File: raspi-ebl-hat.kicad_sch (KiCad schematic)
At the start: 3 parts, among them J1 43045-1012, J2 43650-0515, J3 43650-0615

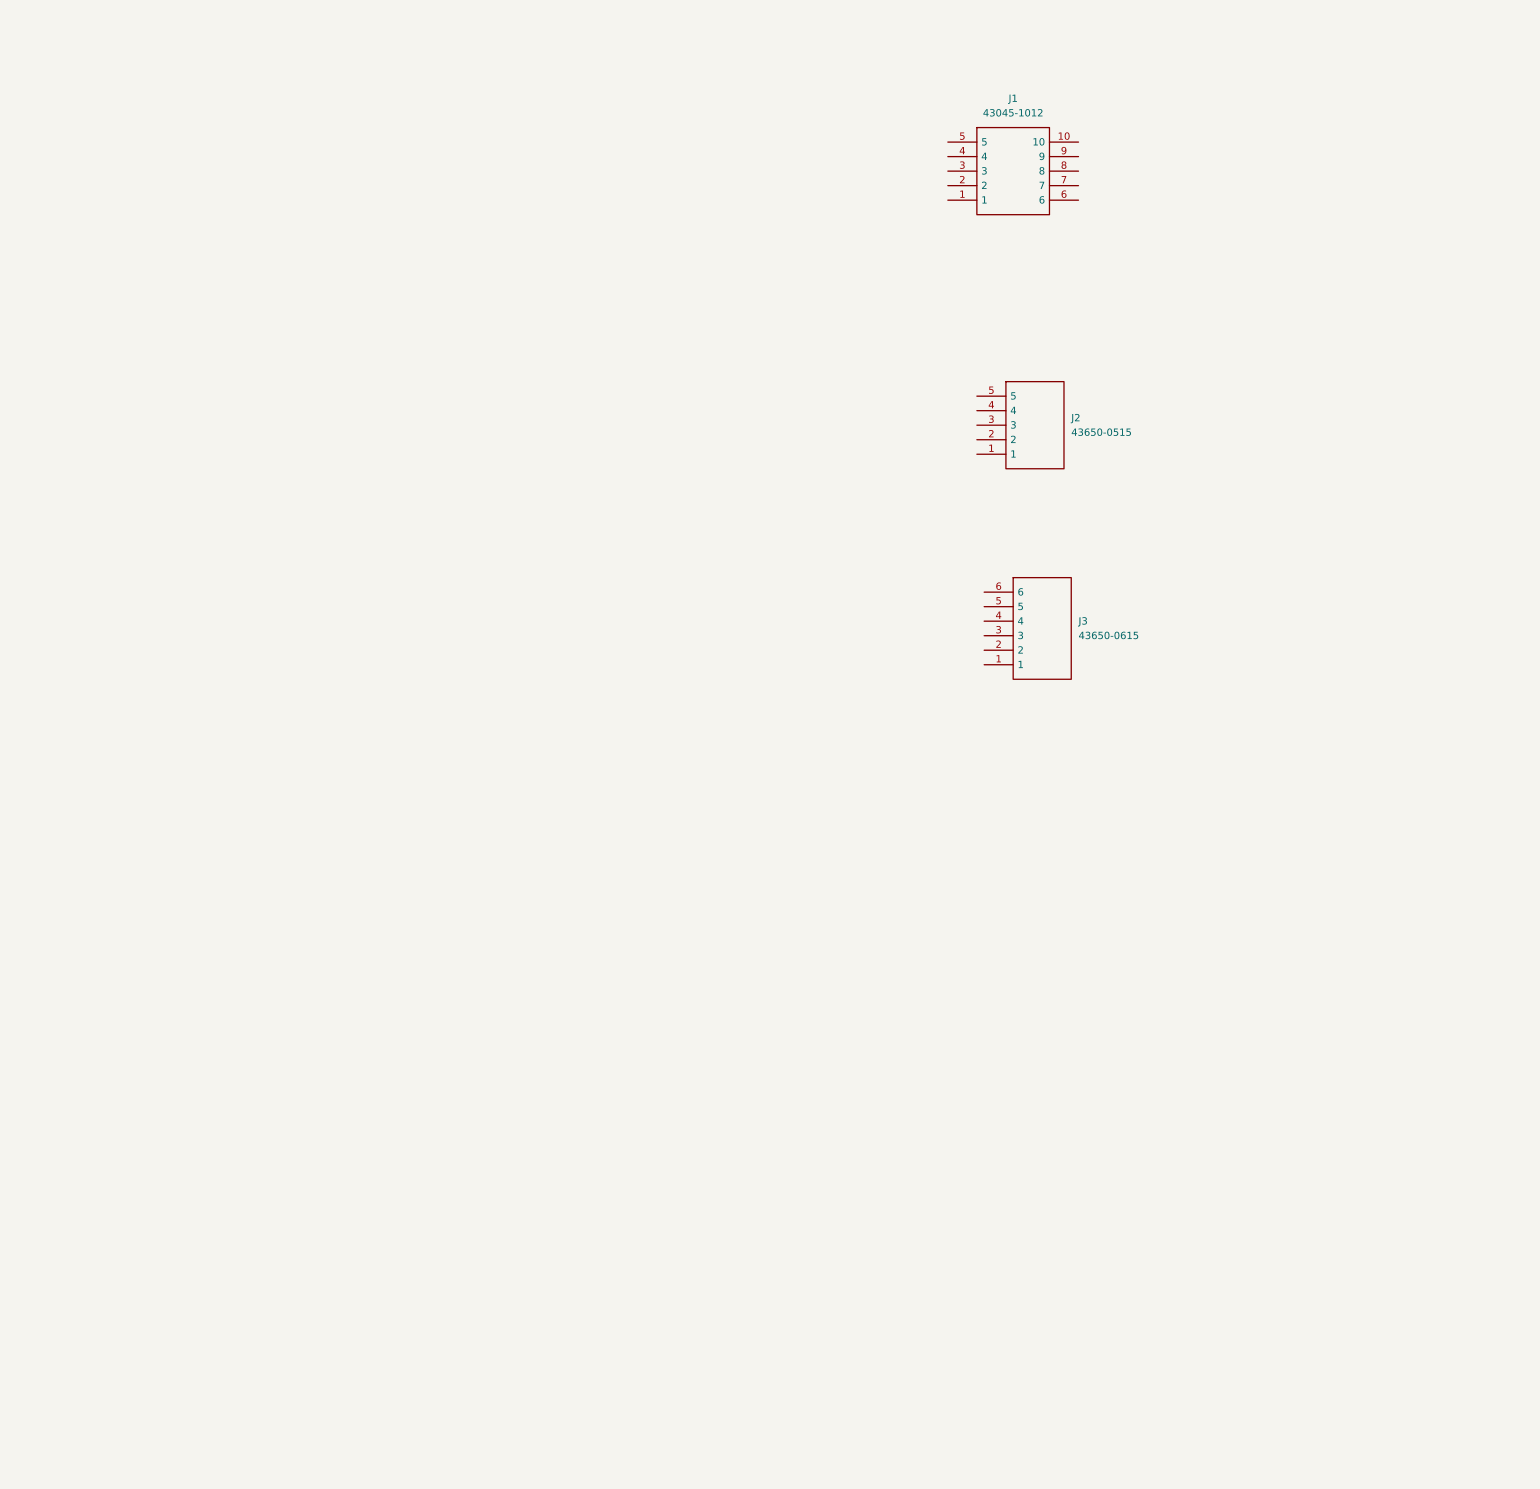
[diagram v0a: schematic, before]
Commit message: imported pihat-template stuff
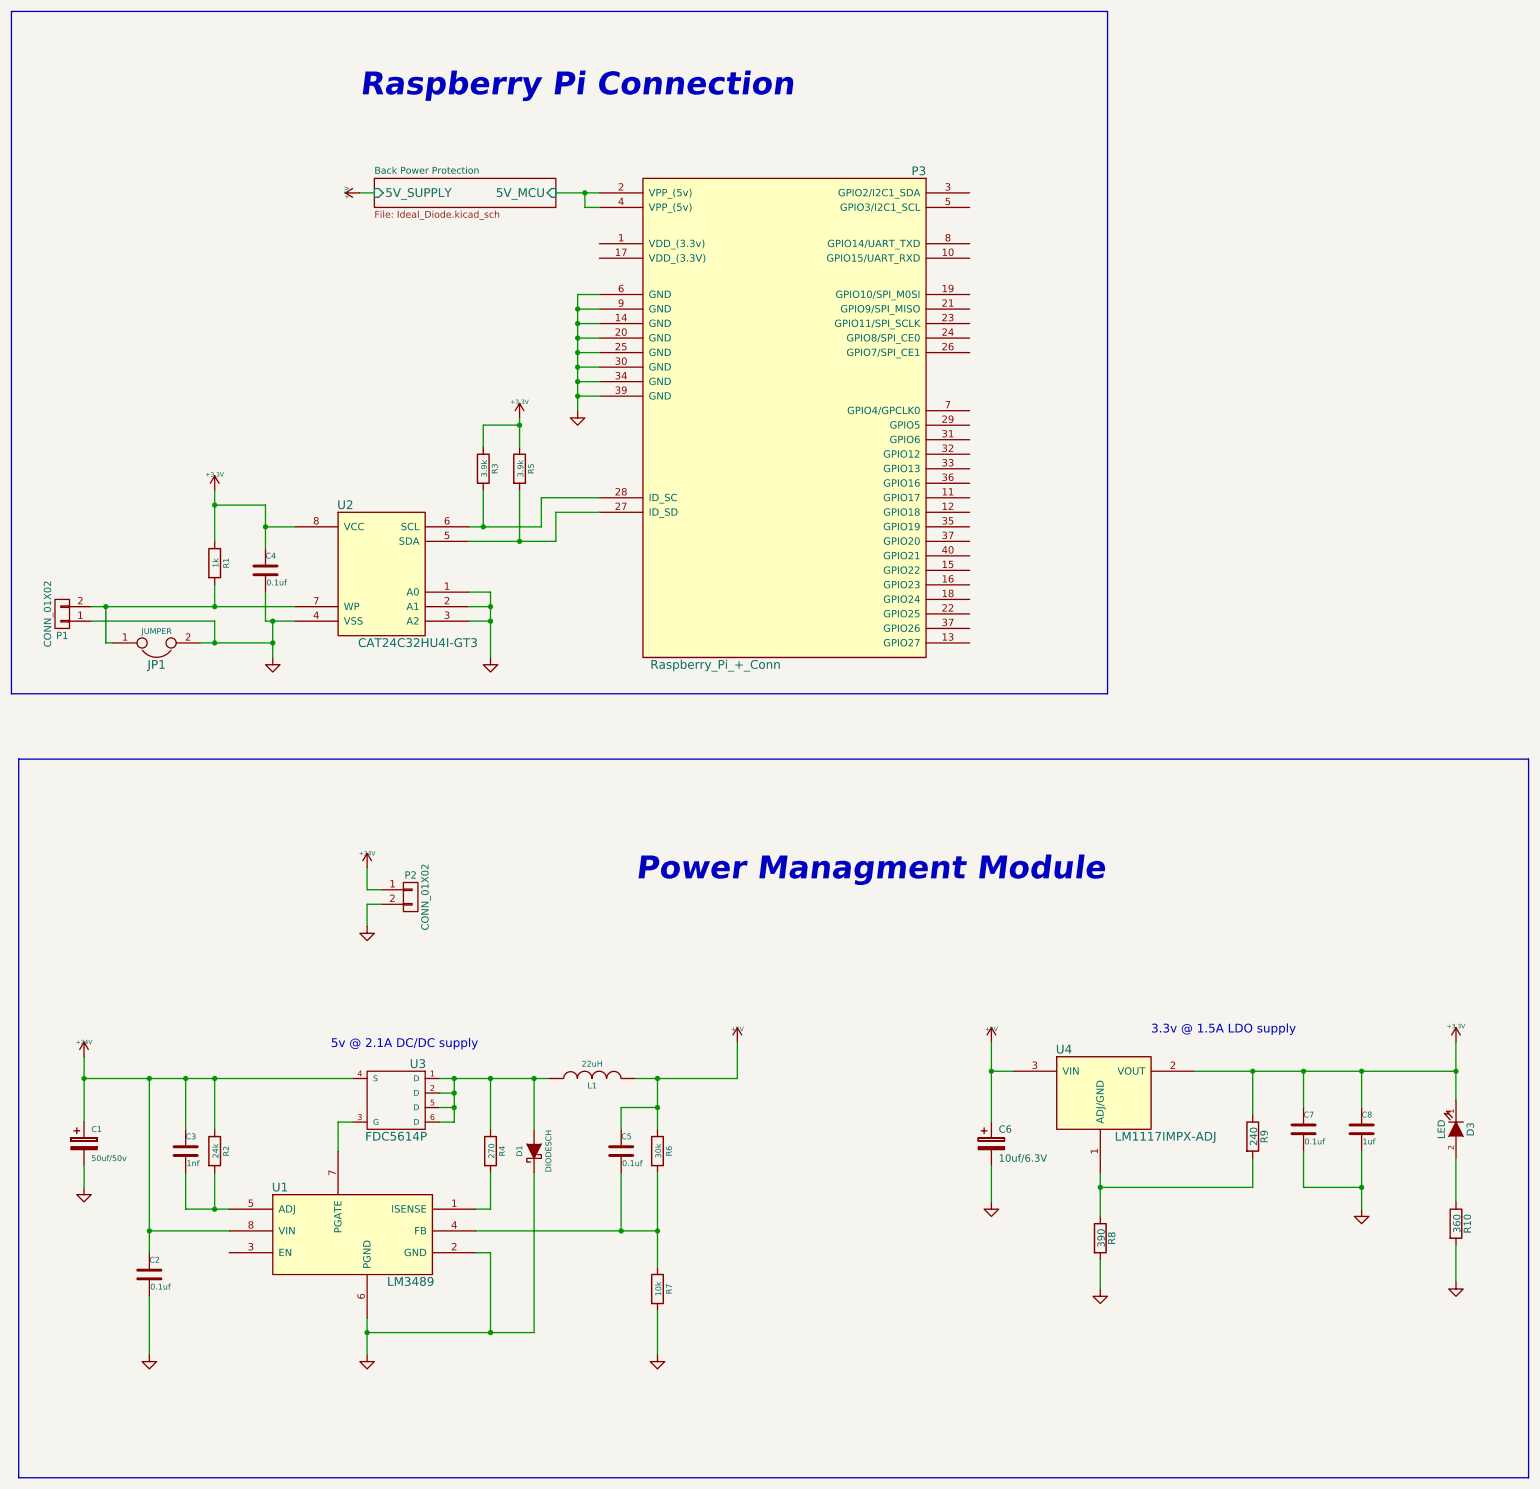
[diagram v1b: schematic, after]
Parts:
- removed J1: 43045-1012, 43045-10YY_12,13,14, symbol parts:43045-1012
- removed J2: 43650-0515, 43650-05YY_15,16,17, symbol parts:43650-0515
- removed J3: 43650-0615, 43650-06YY_15,16,17, symbol parts:43650-0615
- added C1: 50uf/50v, w_smd_cap:c_elec_6.3x7.7, symbol pihat_template-rescue:CP
- added C2, C4, C5, C7: 0.1uf, w_smd_cap:c_0402, symbol pihat_template-rescue:C
- added C3: 1nf, w_smd_cap:c_0402, symbol pihat_template-rescue:C
- added C6: 10uf/6.3V, w_smd_cap:c_elec_4x5.3, symbol pihat_template-rescue:CP
- added C8: 1uf, w_smd_cap:c_0402, symbol pihat_template-rescue:C
- added D1: DIODESCH, w_smd_diode:do214aa, symbol pihat_template-rescue:D_Schottky
- added D3: LED, w_smd_leds:Led_0603, symbol pihat_template-rescue:LED
- added JP1: JUMPER, w_smd_resistors:r_0603, symbol pihat_template-rescue:JUMPER
- added L1: 22uH, w_smd_inductors:inductor_smd_8x5mm, symbol pihat_template-rescue:INDUCTOR
- added P1: CONN_01X02, w_pin_strip:pin_strip_2, symbol pihat_template-rescue:CONN_01X02
- added P2: CONN_01X02, w_conn_mkds:mkds_1,5-2, symbol pihat_template-rescue:CONN_01X02
- added P3: Raspberry_Pi_+_Conn, w_conn_strip:vasch_strip_20x2, symbol pihat_template-rescue:Raspberry_Pi_+_Conn
- added R1: 1k, w_smd_resistors:r_0402, symbol pihat_template-rescue:R
- added R10: 360, w_smd_resistors:r_0402, symbol pihat_template-rescue:R
- added R2: 24k, w_smd_resistors:r_0402, symbol pihat_template-rescue:R
- added R3, R5: 3.9k, w_smd_resistors:r_0402, symbol pihat_template-rescue:R
- added R4: 270, w_smd_resistors:r_0402, symbol pihat_template-rescue:R
- added R6: 30k, w_smd_resistors:r_0402, symbol pihat_template-rescue:R
- added R7: 10k, w_smd_resistors:r_0402, symbol pihat_template-rescue:R
- added R8: 390, w_smd_resistors:r_0402, symbol pihat_template-rescue:R
- added R9: 240, w_smd_resistors:r_0402, symbol pihat_template-rescue:R
- added U1: LM3489, w_smd_dil:msoic-8, symbol pihat_template-rescue:LM3489
- added U2: CAT24C32HU4I-GT3, w_smd_dil:tssop-8, symbol pihat_template-rescue:CAT24C32HU4I-GT3
- added U3: FDC5614P, w_smd_trans:sot23-6, symbol pihat_template-rescue:FDC5614P
- added U4: LM1117IMPX-ADJ, w_smd_trans:sot223, symbol pihat_template-rescue:LM1117IMPX-ADJ
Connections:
- new net: P3.27 (ID_SD), R5.2, U2.5 (SDA)
- new net: P3.28 (ID_SC), R3.2, U2.6 (SCL)
- new net: JP1.1, P1.2 (P2), R1.2, U2.7 (WP)
- new net: R4.2, U1.1 (ISENSE)
- new net: C5.2, R6.2, R7.1, U1.4 (FB)
- new net: C3.2, R2.2, U1.5 (ADJ)
- new net: U1.7 (PGATE), U3.3 (G)
- new net: D1.2 (A), L1.1, R4.1, U3.1 (D), U3.2 (D), U3.5 (D), U3.6 (D)
- new net: R8.1, R9.2, U4.1 (ADJ/GND)
- new net: D3.2 (A), R10.1
- new net +24V: C1.1, C2.1, C3.1, P2.1 (P1), R2.1, U1.8 (VIN), U3.4 (S)
- new net +3V3: C4.1, C7.1, C8.1, D3.1 (K), R1.1, R3.1, R5.1, R9.1, U2.8 (VCC), U4.2 (VOUT)
- new net +5V: C5.1, C6.1, L1.2, R6.1, U4.3 (VIN)
- new net Back Power Protection/5V_MCU: P3.2 (VPP_(5v)), P3.4 (VPP_(5v))
- new net GND: C1.2, C2.2, C4.2, C6.2, C7.2, C8.2, D1.1 (K), JP1.2, P1.1 (P1), P2.2 (P2), P3.14 (GND), P3.20 (GND), P3.25 (GND), P3.30 (GND), P3.34 (GND), P3.39 (GND), P3.6 (GND), P3.9 (GND), R10.2, R7.2, R8.2, U1.2 (GND), U1.6 (PGND), U2.1 (A0), U2.2 (A1), U2.3 (A2), U2.4 (VSS)
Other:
- added sheet Back Power Protection (Ideal_Diode.kicad_sch)
- note added: "3.3v @ 1.5A LDO supply"
- note added: "5v @ 2.1A DC/DC supply"
- note added: "Power Managment Module"
- note added: "Raspberry Pi Connection"
